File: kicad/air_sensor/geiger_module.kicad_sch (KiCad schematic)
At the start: 7 parts, among them U4 ATtiny412

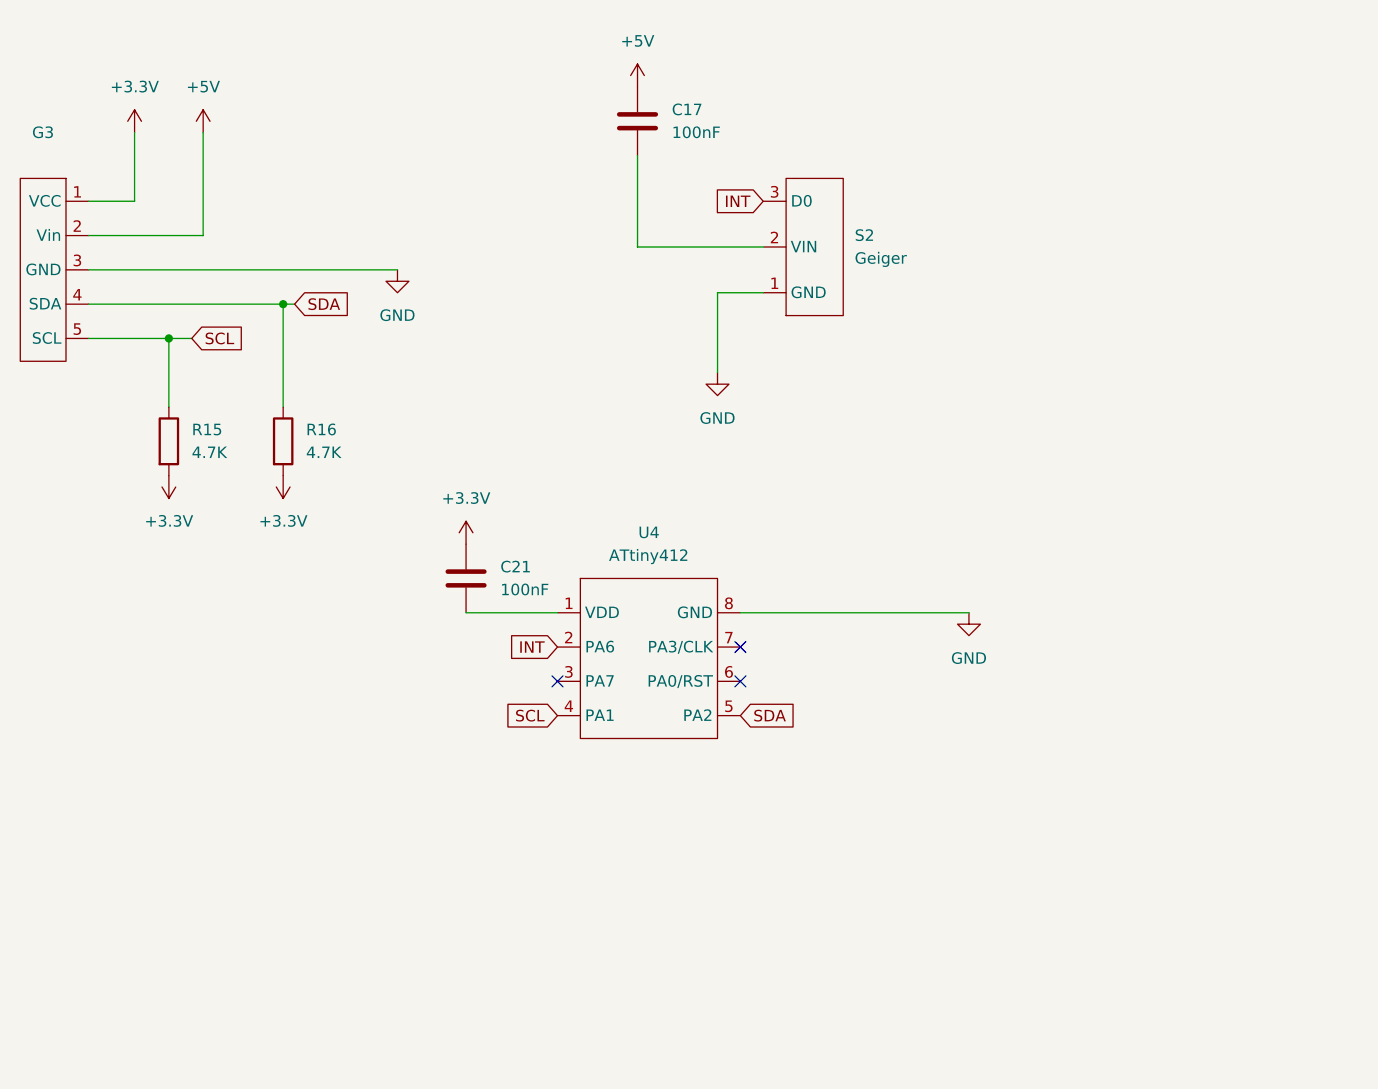
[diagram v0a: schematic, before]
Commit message: updated schema
added 5V 3A buck converter
refined 3v3 LDO
added symbols for new components
added text comments for designing the pcb
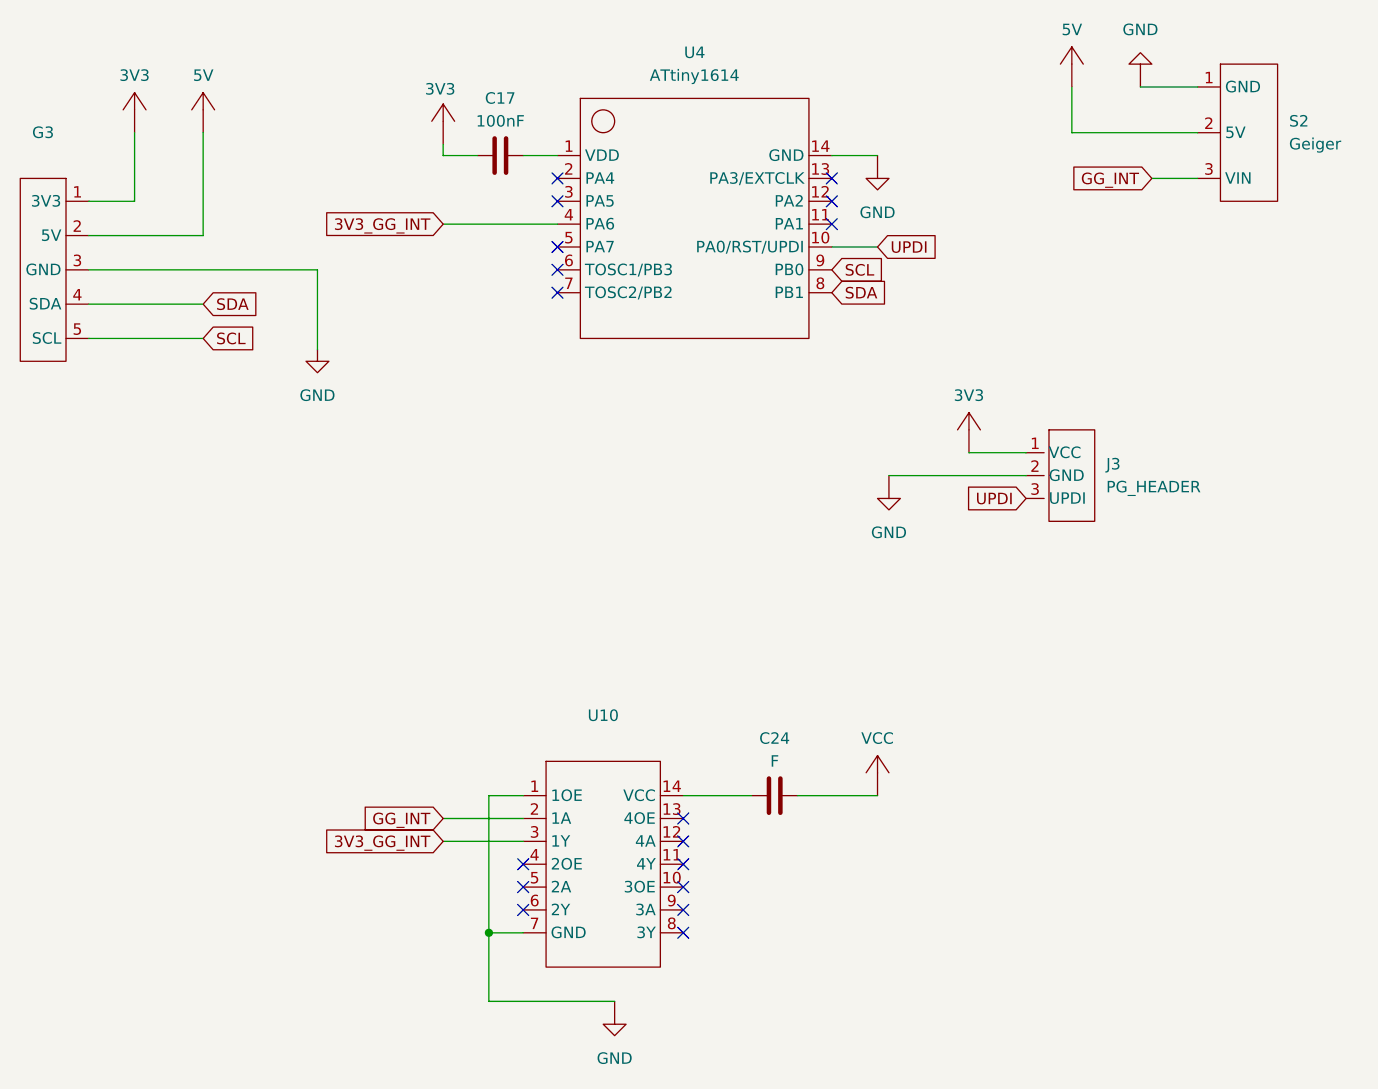
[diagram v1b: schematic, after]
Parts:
- removed C17, C21: 100nF, symbol Device:C
- removed R15, R16: 4.7K, symbol Device:R
- removed U4: ATtiny412, symbol air_sens_lib:ATtiny412
- added C17: 100nF, symbol common:Capacitor
- added C24: F, symbol common:Capacitor
- added J3: PG_HEADER, symbol air_sens_lib:ATtiny1614_programming_header
- added U10: ~, symbol air_sens_lib:SN74LVC125
- added U4: ATtiny1614, symbol air_sens_lib:ATtiny1614
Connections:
- net +5V is gone; now on net 5V: G3.2 (5V)
- net GND: now also J3.2 (GND), U10.1 (1OE), U10.7 (GND), U4.14 (GND)
- net SCL: now also U4.9 (PB0)
- net SDA: now also U4.8 (PB1)
- net 5V: now reaches S2.2 (5V)
- net +3.3V renamed 3V3
- net 3V3: now also C17.1, J3.1 (VCC)
- net INT renamed GG_INT
- net GG_INT: now also U10.2 (1A)
- new net: C17.2, U4.1 (VDD)
- new net: C24.1, U10.14 (VCC)
- new net 3V3_GG_INT: U10.3 (1Y), U4.4 (PA6)
- new net UPDI: J3.3 (UPDI), U4.10 (PA0/RST/UPDI)
- new net VCC: C24.2
- no-connect marks 3 -> 17

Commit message: updated power symbol labels, replaced power symbols in schematic with our own custom symbols
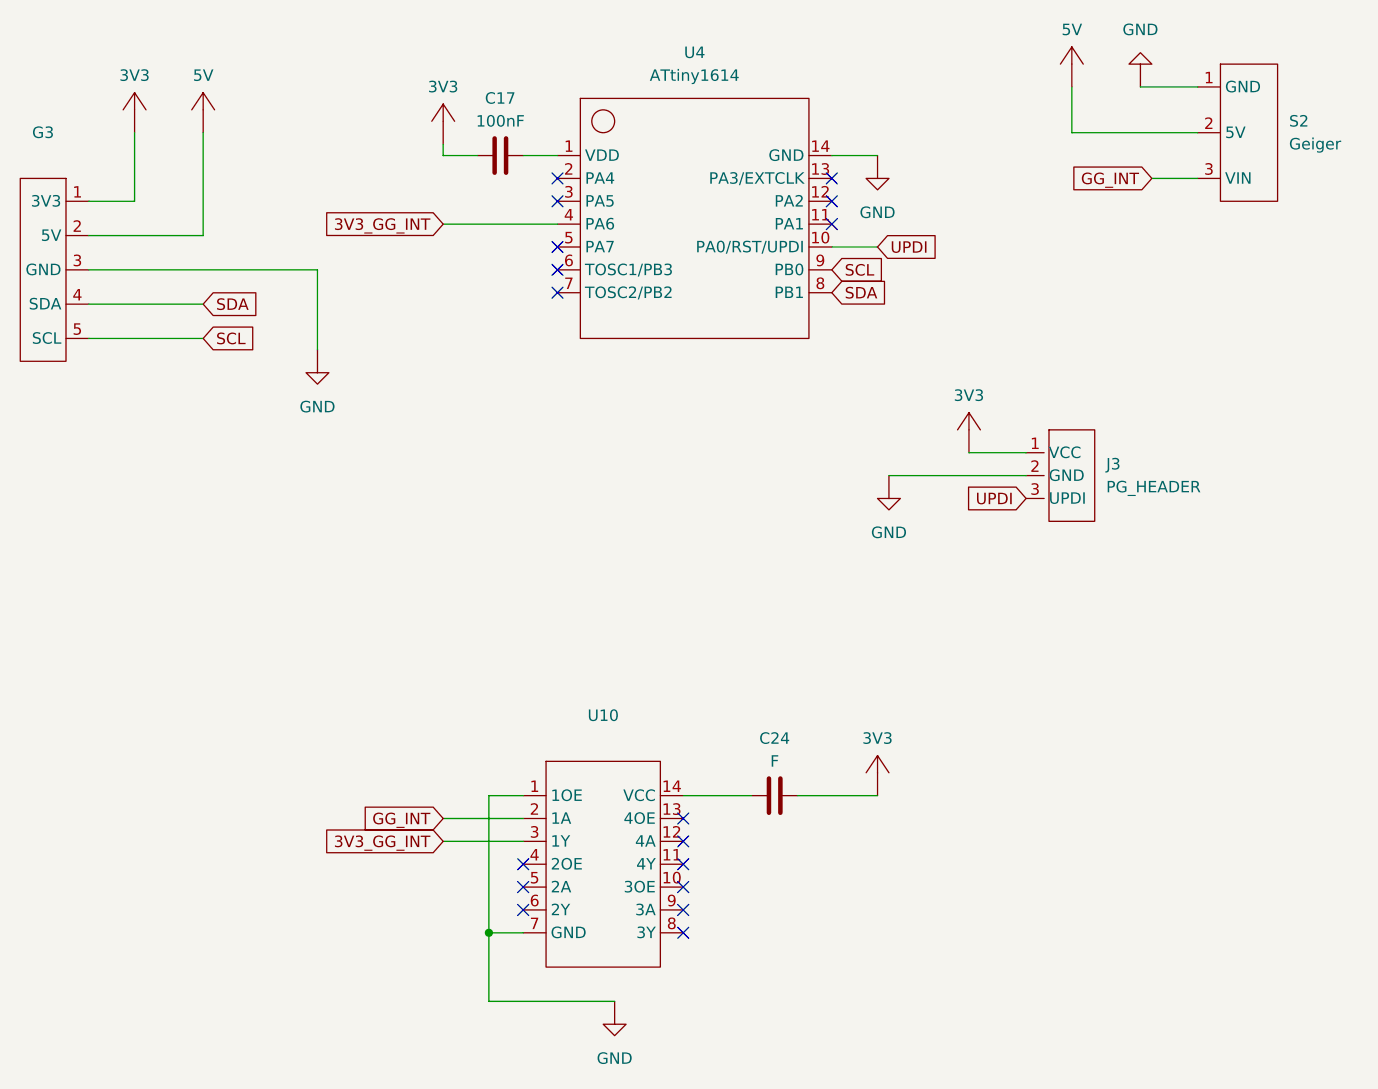
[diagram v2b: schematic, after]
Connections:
- net VCC is gone; now on net 3V3: C24.2
